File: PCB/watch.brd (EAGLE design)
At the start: 81.1 x 53.1 mm, 58 parts, among them IC1 ISL1209, J2 USB-MICROB, Q1 32.768 KHz, T1 BC850, U2 MKL27Z256VLH4

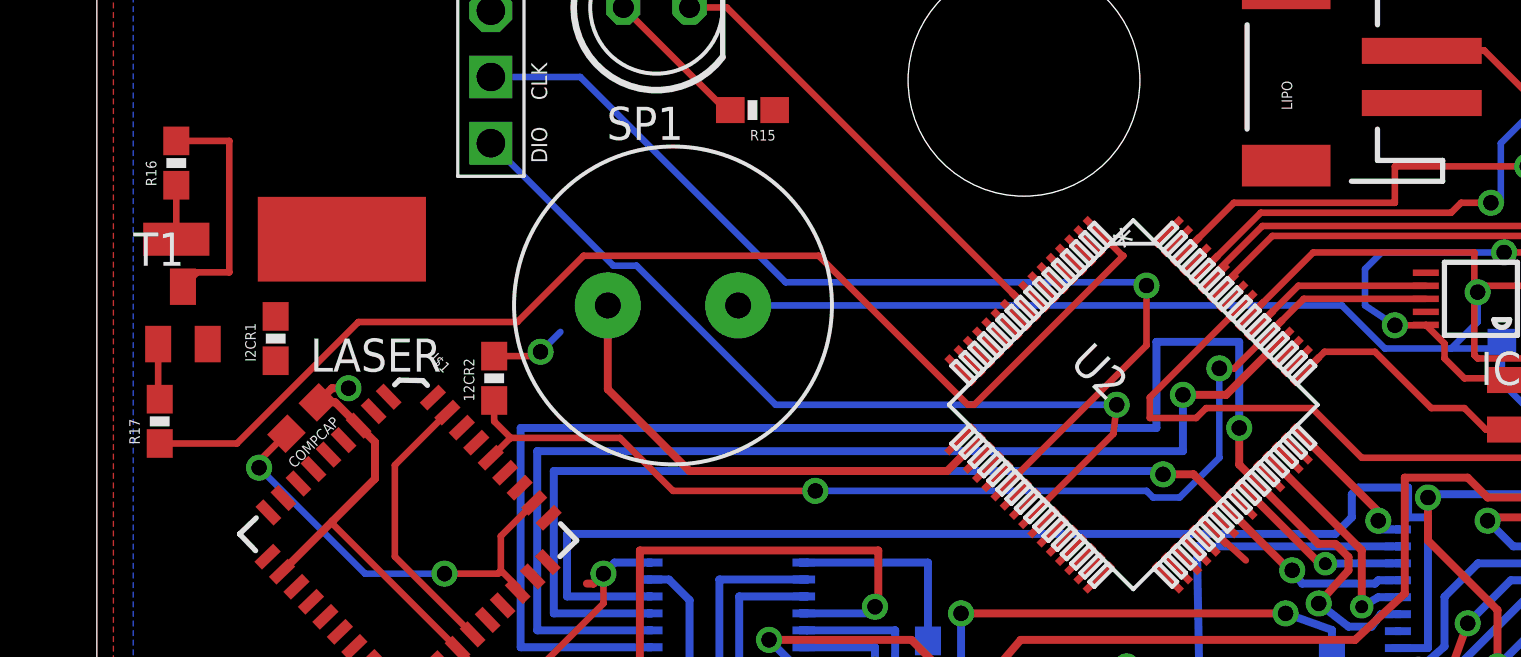
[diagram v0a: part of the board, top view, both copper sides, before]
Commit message: fixed mroe air wires
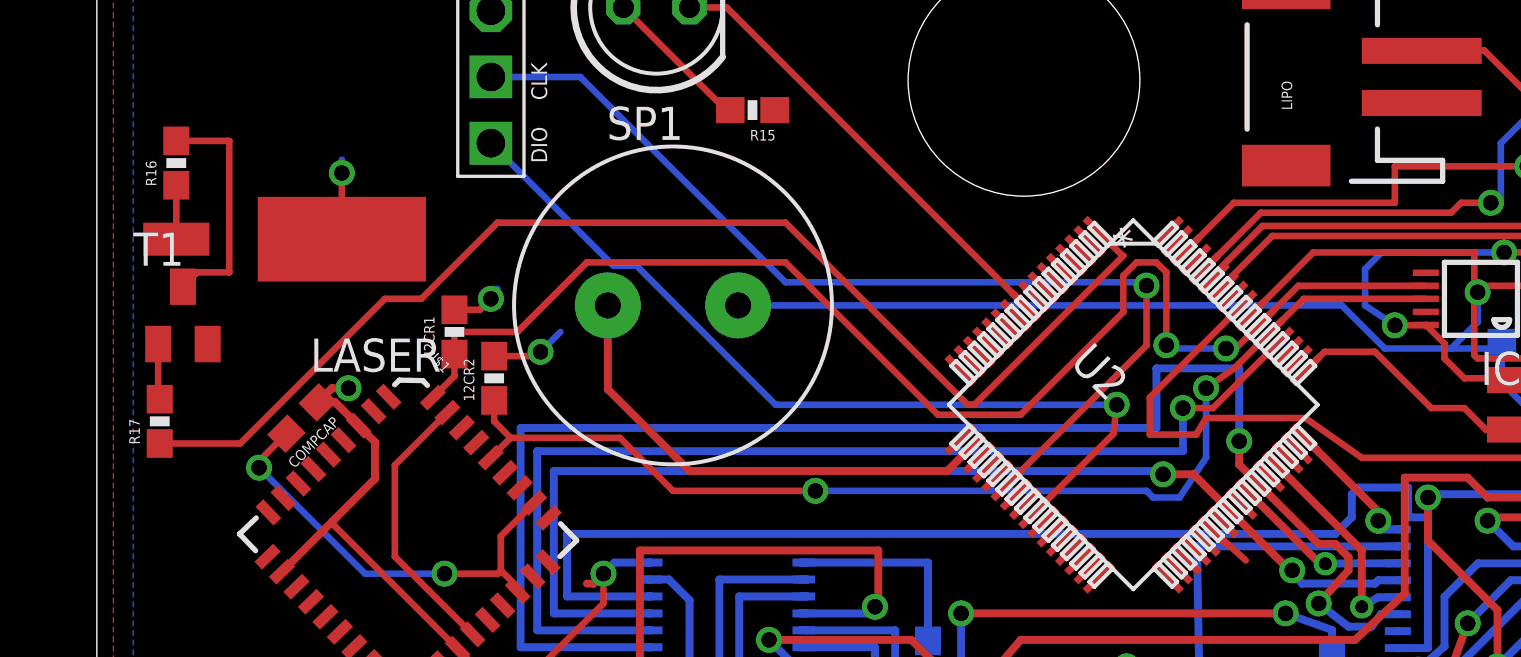
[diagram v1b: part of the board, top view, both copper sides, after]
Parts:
- moved I2CR1 6.86 mm to (24.6, 44.7)
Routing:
- net PTC9: track 6.97 -> 51.0 mm, vias 0 -> 2
- net V+: track 60.1 -> 65.2 mm, vias 7 -> 9
- net PTC0: track 60.0 -> 58.0 mm
- net PTE0: track 46.0 -> 47.0 mm
- net PTC11: track 33.5 -> 34.0 mm

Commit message: wired decoupling caps
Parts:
- moved C6 113.6 mm to (49.8, 48.4), flipped to the bottom, turned to 90 degrees
- moved C5 104.4 mm to (43.6, 46.1), turned to 43.8 degrees
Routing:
- net V+: track 65.2 -> 87.4 mm, vias 9 -> 12
- net GND: track 97.2 -> 113.9 mm, vias 11 -> 13
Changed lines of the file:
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@@
 <attribute name="PROD_ID" value="CAP-00810" x="79.121" y="52.451" size="1.778" layer="27" rot="R90" display="off"/>
 </element>
-<element name="C5" library="SparkFun" package="0603" value=".1uf" x="-57.15" y="73.66"/>
-<element name="C6" library="SparkFun" package="0603" value=".1uf" x="-60.96" y="73.66"/>
+<element name="C5" library="SparkFun" package="0603" value=".1uf" x="43.561" y="46.101" rot="R43.8"/>
+<element name="C6" library="SparkFun" package="0603" value=".1uf" x="49.784" y="48.387" rot="MR90"/>
 <element name="C7" library="SparkFun" package="0603" value=".1uf" x="-64.77" y="73.66"/>
 <element name="C8" library="SparkFun" package="0603" value=".1uf" x="-68.58" y="73.66"/>
@@
 <wire x1="24.257" y1="35.433" x2="26.289" y2="35.433" width="0.254" layer="1"/>
 <wire x1="26.289" y1="35.433" x2="26.416" y2="35.56" width="0.254" layer="1" curve="90"/>
+<wire x1="49.784" y1="47.537" x2="46.189" y2="47.537" width="0.254" layer="16"/>
+<wire x1="46.189" y1="47.537" x2="45.72" y2="48.006" width="0.254" layer="16"/>
+<via x="45.72" y="48.006" extent="1-16" drill="0.6"/>
+<wire x1="45.72" y1="48.006" x2="47.758990625" y2="48.006" width="0.254" layer="1"/>
+<wire x1="47.758990625" y1="48.006" x2="48.286515625" y2="47.478475" width="0.254" layer="1"/>
+<wire x1="42.947503125" y1="45.512678125" x2="42.625321875" y2="45.512678125" width="0.254" layer="1"/>
+<wire x1="42.625321875" y1="45.512678125" x2="40.259" y2="47.879" width="0.254" layer="1"/>
+<via x="40.259" y="47.879" extent="1-16" drill="0.6"/>
+<wire x1="40.259" y1="47.879" x2="41.275" y2="48.768" width="0.254" layer="16"/>
+<wire x1="41.275" y1="48.768" x2="44.196" y2="48.768" width="0.254" layer="16"/>
+<wire x1="44.196" y1="48.768" x2="45.085" y2="48.006" width="0.254" layer="16"/>
+<wire x1="45.085" y1="48.006" x2="45.72" y2="48.006" width="0.254" layer="16"/>
 <wire x1="60.325" y1="44.069" x2="56.94858125" y2="40.23061875" width="0" layer="19" extent="1-16"/>
 <wire x1="48.99361875" y1="35.634415625" x2="56.94858125" y2="40.23061875" width="0" layer="19" extent="1-1"/>
-<wire x1="48.286515625" y1="47.478475" x2="58.674" y2="45.72" width="0" layer="19" extent="1-16"/>
-<wire x1="-58" y1="73.66" x2="15.174" y2="44.239" width="0" layer="19" extent="1-1"/>
-<wire x1="-61.81" y1="73.66" x2="-58" y2="73.66" width="0" layer="19" extent="1-1"/>
-<wire x1="-65.62" y1="73.66" x2="-61.81" y2="73.66" width="0" layer="19" extent="1-1"/>
+<wire x1="-65.62" y1="73.66" x2="15.174" y2="44.239" width="0" layer="19" extent="1-1"/>
 <wire x1="-69.43" y1="73.66" x2="-65.62" y2="73.66" width="0" layer="19" extent="1-1"/>
 </signal>
@@
 <via x="20.32" y="50.8" extent="1-16" drill="0.6"/>
 <wire x1="20.32" y1="50.8" x2="20.32" y2="51.308" width="0.254" layer="16"/>
-<wire x1="45.104521875" y1="44.29648125" x2="48.640065625" y2="47.832028125" width="0" layer="19" extent="1-1"/>
-<wire x1="48.640065625" y1="35.98796875" x2="45.104521875" y2="44.29648125" width="0" layer="19" extent="1-1"/>
-<wire x1="57.302134375" y1="40.584171875" x2="48.640065625" y2="35.98796875" width="0" layer="19" extent="1-1"/>
-<wire x1="60.706" y1="44.958" x2="57.302134375" y2="40.584171875" width="0" layer="19" extent="1-16"/>
+<wire x1="44.17449375" y1="46.68931875" x2="44.17449375" y2="45.226509375" width="0.254" layer="1"/>
+<wire x1="44.17449375" y1="45.226509375" x2="45.104521875" y2="44.29648125" width="0.254" layer="1"/>
+<wire x1="44.17449375" y1="46.68931875" x2="44.11568125" y2="46.68931875" width="0.254" layer="1"/>
+<wire x1="44.11568125" y1="46.68931875" x2="42.799" y2="48.006" width="0.254" layer="1"/>
+<via x="42.799" y="48.006" extent="1-16" drill="0.6"/>
+<wire x1="42.799" y1="48.006" x2="42.545" y2="48.26" width="0.254" layer="16"/>
+<wire x1="49.784" y1="49.237" x2="47.332" y2="49.237" width="0.254" layer="16"/>
+<wire x1="47.332" y1="49.237" x2="47.244" y2="49.149" width="0.254" layer="16"/>
+<via x="47.244" y="49.149" extent="1-16" drill="0.6"/>
+<wire x1="47.244" y1="49.149" x2="47.32309375" y2="49.149" width="0.254" layer="1"/>
+<wire x1="47.32309375" y1="49.149" x2="48.640065625" y2="47.832028125" width="0.254" layer="1"/>
+<wire x1="44.17449375" y1="46.68931875" x2="40.513" y2="50.3508125" width="0.254" layer="1"/>
+<wire x1="40.513" y1="50.3508125" x2="40.513" y2="50.419" width="0.254" layer="1"/>
+<via x="40.513" y="50.419" extent="1-16" drill="0.6"/>
+<wire x1="40.513" y1="50.419" x2="40.64" y2="50.546" width="0.254" layer="16"/>
+<wire x1="40.64" y1="50.546" x2="42.545" y2="50.546" width="0.254" layer="16"/>
+<wire x1="42.545" y1="50.546" x2="43.942" y2="49.149" width="0.254" layer="16"/>
+<wire x1="43.942" y1="49.149" x2="47.244" y2="49.149" width="0.254" layer="16"/>
+<wire x1="45.104521875" y1="44.29648125" x2="48.640065625" y2="35.98796875" width="0" layer="19" extent="1-1"/>
+<wire x1="57.302134375" y1="40.584171875" x2="60.706" y2="44.958" width="0" layer="19" extent="1-16"/>
 <wire x1="41.822" y1="16.002" x2="48.640065625" y2="35.98796875" width="0" layer="19" extent="1-1"/>
 <wire x1="43.649" y1="13.335" x2="41.822" y2="16.002" width="0" layer="19" extent="1-1"/>
@@
 <wire x1="63.666" y1="12.954" x2="43.649" y2="13.335" width="0" layer="19" extent="1-1"/>
 <wire x1="63.666" y1="16.002" x2="63.666" y2="12.954" width="0" layer="19" extent="1-1"/>
-<wire x1="-56.3" y1="73.66" x2="20.32" y2="51.308" width="0" layer="19" extent="1-16"/>
-<wire x1="-60.11" y1="73.66" x2="-56.3" y2="73.66" width="0" layer="19" extent="1-1"/>
-<wire x1="-63.92" y1="73.66" x2="-60.11" y2="73.66" width="0" layer="19" extent="1-1"/>
+<wire x1="-63.92" y1="73.66" x2="20.32" y2="51.308" width="0" layer="19" extent="1-16"/>
 <wire x1="-67.73" y1="73.66" x2="-63.92" y2="73.66" width="0" layer="19" extent="1-1"/>
 </signal>

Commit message: moved IR for smaller form factor
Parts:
- moved LED-IR 4.20 mm to (36.2, 55.4)
- moved R15 3.74 mm to (39.1, 51.1), turned to 270 degrees
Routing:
- net PTE20: track 17.6 -> 13.4 mm
- net N$39: track 5.73 -> 8.71 mm
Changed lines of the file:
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@@
 <element name="LASER" library="Photonics" package="LD-FLUSH-WITH-JUMPER" value="LD" x="20.32" y="48.26" rot="R180"/>
 <element name="LED-E" library="led" package="LED5MM" value="" x="87.884" y="18.034"/>
-<element name="LED-IR" library="led" package="LED5MM" value="" x="32.385" y="57.15"/>
+<element name="LED-IR" library="led" package="LED5MM" value="" x="36.195" y="55.372"/>
 <element name="LED-N" library="led" package="LED5MM" value="" x="82.169" y="26.289"/>
 <element name="LED-S" library="led" package="LED5MM" value="" x="82.169" y="10.922"/>
@@
 <element name="R13" library="SparkFun-Resistors" package="0603-RES" value="220Ohm" x="89.027" y="9.271" rot="R180"/>
 <element name="R14" library="SparkFun-Resistors" package="0603-RES" value="220Ohm" x="72.644" y="12.827" rot="R90"/>
-<element name="R15" library="SparkFun-Resistors" package="0603-RES" value="220Ohm" x="36.068" y="53.213" rot="R180"/>
+<element name="R15" library="SparkFun-Resistors" package="0603-RES" value="220Ohm" x="39.116" y="51.054" rot="R270"/>
 <element name="R16" library="SparkFun-Resistors" package="0603-RES" value="10" x="13.97" y="51.181" rot="R90"/>
 <element name="R17" library="SparkFun-Resistors" package="0603-RES" value="10K" x="13.335" y="41.275" rot="R90"/>
@@
 <contactref element="U2" pad="9"/>
 <contactref element="LED-IR" pad="K"/>
-<wire x1="33.655" y1="57.15" x2="35.079459375" y2="57.15" width="0.254" layer="1"/>
-<wire x1="35.079459375" y1="57.15" x2="46.51875" y2="45.710709375" width="0.254" layer="1"/>
+<wire x1="37.465" y1="55.372" x2="44.831" y2="48.006" width="0.254" layer="1"/>
+<wire x1="44.831" y1="48.006" x2="44.831" y2="47.398459375" width="0.254" layer="1"/>
+<wire x1="44.831" y1="47.398459375" x2="46.51875" y2="45.710709375" width="0.254" layer="1"/>
 </signal>
 <signal name="PTA13">
@@
 <contactref element="R15" pad="2"/>
 <contactref element="LED-IR" pad="A"/>
-<wire x1="31.115" y1="57.15" x2="35.052" y2="53.213" width="0.254" layer="1"/>
-<wire x1="35.052" y1="53.213" x2="35.218" y2="53.213" width="0.254" layer="1"/>
+<wire x1="34.925" y1="55.372" x2="34.925" y2="51.308" width="0.254" layer="1"/>
+<wire x1="34.925" y1="51.308" x2="35.941" y2="50.292" width="0.254" layer="1"/>
+<wire x1="35.941" y1="50.292" x2="39.028" y2="50.292" width="0.254" layer="1"/>
+<wire x1="39.028" y1="50.292" x2="39.116" y2="50.204" width="0.254" layer="1"/>
 </signal>
 <signal name="PTA12">

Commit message: all but one decoup cap done
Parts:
- moved C8 128.9 mm to (56.4, 42.0), flipped to the bottom, turned to 135 degrees
- moved C7 116.5 mm to (45.2, 35.3)
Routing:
- net V+: track 87.4 -> 107.6 mm
- net GND: track 113.9 -> 133.0 mm
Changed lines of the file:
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@@
 <element name="C5" library="SparkFun" package="0603" value=".1uf" x="43.561" y="46.101" rot="R43.8"/>
 <element name="C6" library="SparkFun" package="0603" value=".1uf" x="49.784" y="48.387" rot="MR90"/>
-<element name="C7" library="SparkFun" package="0603" value=".1uf" x="-64.77" y="73.66"/>
-<element name="C8" library="SparkFun" package="0603" value=".1uf" x="-68.58" y="73.66"/>
+<element name="C7" library="SparkFun" package="0603" value=".1uf" x="45.212" y="35.306"/>
+<element name="C8" library="SparkFun" package="0603" value=".1uf" x="56.388" y="42.037" rot="MR135"/>
 <element name="COMPCAP" library="SparkFun" package="0603" value=".1uf" x="18.796" y="41.402" rot="R225"/>
 <element name="DISP1" library="SparkFun-Displays" package="DIL12" value="7-SEGMENT-4DIGIT-COUNTER-HP-BUBBLE" x="44.069" y="25.273">
@@
 <wire x1="44.196" y1="48.768" x2="45.085" y2="48.006" width="0.254" layer="16"/>
 <wire x1="45.085" y1="48.006" x2="45.72" y2="48.006" width="0.254" layer="16"/>
+<wire x1="44.958" y1="34.417" x2="47.776203125" y2="34.417" width="0.254" layer="1"/>
+<wire x1="47.776203125" y1="34.417" x2="48.99361875" y2="35.634415625" width="0.254" layer="1"/>
+<wire x1="44.362" y1="35.306" x2="44.362" y2="35.013" width="0.254" layer="1"/>
+<wire x1="44.362" y1="35.013" x2="44.958" y2="34.417" width="0.254" layer="1"/>
+<wire x1="44.362" y1="35.013" x2="43.18" y2="35.013" width="0.254" layer="1"/>
+<wire x1="43.18" y1="35.013" x2="43.18" y2="33.401" width="0.254" layer="1"/>
+<wire x1="43.18" y1="33.401" x2="37.465" y2="33.401" width="0.254" layer="1"/>
+<wire x1="37.465" y1="33.401" x2="36.957" y2="33.909" width="0.254" layer="1"/>
+<wire x1="36.957" y1="33.909" x2="35.941" y2="33.909" width="0.254" layer="1"/>
+<wire x1="35.941" y1="33.909" x2="35.56" y2="33.528" width="0.254" layer="1"/>
+<wire x1="35.56" y1="33.528" x2="35.56" y2="31.877" width="0.254" layer="1"/>
+<wire x1="35.56" y1="31.877" x2="35.814" y2="31.623" width="0.254" layer="1"/>
+<wire x1="35.814" y1="31.623" x2="36.449" y2="31.623" width="0.254" layer="1"/>
 <wire x1="60.325" y1="44.069" x2="56.94858125" y2="40.23061875" width="0" layer="19" extent="1-16"/>
-<wire x1="48.99361875" y1="35.634415625" x2="56.94858125" y2="40.23061875" width="0" layer="19" extent="1-1"/>
-<wire x1="-65.62" y1="73.66" x2="15.174" y2="44.239" width="0" layer="19" extent="1-1"/>
-<wire x1="-69.43" y1="73.66" x2="-65.62" y2="73.66" width="0" layer="19" extent="1-1"/>
+<wire x1="55.786959375" y1="41.43595625" x2="15.174" y2="44.239" width="0" layer="19" extent="1-1"/>
 </signal>
 <signal name="V+">
@@
 <wire x1="42.545" y1="50.546" x2="43.942" y2="49.149" width="0.254" layer="16"/>
 <wire x1="43.942" y1="49.149" x2="47.244" y2="49.149" width="0.254" layer="16"/>
-<wire x1="45.104521875" y1="44.29648125" x2="48.640065625" y2="35.98796875" width="0" layer="19" extent="1-1"/>
+<wire x1="47.958096875" y1="35.306" x2="48.640065625" y2="35.98796875" width="0.254" layer="1"/>
+<wire x1="46.062" y1="35.306" x2="47.958096875" y2="35.306" width="0.254" layer="1"/>
+<wire x1="46.062" y1="35.306" x2="44.538" y2="36.83" width="0.254" layer="1"/>
+<wire x1="44.538" y1="36.83" x2="31.115" y2="36.83" width="0.254" layer="1"/>
+<wire x1="31.115" y1="36.83" x2="30.353" y2="36.068" width="0.254" layer="1"/>
+<wire x1="30.353" y1="36.068" x2="30.353" y2="35.433" width="0.254" layer="1"/>
+<wire x1="63.666" y1="12.954" x2="63.666" y2="16.002" width="0" layer="19" extent="1-1"/>
+<wire x1="43.649" y1="13.335" x2="63.666" y2="12.954" width="0" layer="19" extent="1-1"/>
+<wire x1="43.649" y1="10.414" x2="43.649" y2="13.335" width="0" layer="19" extent="1-1"/>
+<wire x1="41.822" y1="16.002" x2="43.649" y2="13.335" width="0" layer="19" extent="1-1"/>
+<wire x1="46.062" y1="35.306" x2="41.822" y2="16.002" width="0" layer="19" extent="1-1"/>
 <wire x1="57.302134375" y1="40.584171875" x2="60.706" y2="44.958" width="0" layer="19" extent="1-16"/>
-<wire x1="41.822" y1="16.002" x2="48.640065625" y2="35.98796875" width="0" layer="19" extent="1-1"/>
-<wire x1="43.649" y1="13.335" x2="41.822" y2="16.002" width="0" layer="19" extent="1-1"/>
-<wire x1="43.649" y1="10.414" x2="43.649" y2="13.335" width="0" layer="19" extent="1-1"/>
-<wire x1="63.666" y1="12.954" x2="43.649" y2="13.335" width="0" layer="19" extent="1-1"/>
-<wire x1="63.666" y1="16.002" x2="63.666" y2="12.954" width="0" layer="19" extent="1-1"/>
-<wire x1="-63.92" y1="73.66" x2="20.32" y2="51.308" width="0" layer="19" extent="1-16"/>
-<wire x1="-67.73" y1="73.66" x2="-63.92" y2="73.66" width="0" layer="19" extent="1-1"/>
+<wire x1="56.98904375" y1="42.638040625" x2="20.32" y2="51.308" width="0" layer="19" extent="1-16"/>
 </signal>
 <signal name="PTA19">
@@
 <wire x1="66.675" y1="39.878" x2="59.436" y2="39.878" width="0.254" layer="1"/>
 <wire x1="59.436" y1="39.878" x2="57.277" y2="41.402" width="0.254" layer="1"/>
-<wire x1="57.277" y1="41.402" x2="53.467" y2="41.402" width="0.254" layer="1"/>
 <wire x1="53.467" y1="41.402" x2="53.086" y2="40.767" width="0.254" layer="1"/>
 <wire x1="53.086" y1="40.767" x2="51.308" y2="40.767" width="0.254" layer="1"/>
@@
 <wire x1="69.215" y1="37.338" x2="69.215" y2="32.85" width="0.254" layer="1"/>
 <wire x1="69.215" y1="32.85" x2="72.51" y2="32.85" width="0.254" layer="1"/>
+<wire x1="57.277" y1="41.402" x2="53.467" y2="41.402" width="0.254" layer="1"/>
 </signal>
 <signal name="PTC4">
@@
 <contactref element="T2" pad="B"/>
 <wire x1="64.94" y1="40.96" x2="64.196" y2="40.96" width="0.254" layer="1"/>
-<wire x1="64.196" y1="40.96" x2="63.373" y2="41.783" width="0.254" layer="1"/>
-<wire x1="63.373" y1="41.783" x2="62.103" y2="41.783" width="0.254" layer="1"/>
 <wire x1="57.302134375" y1="43.235825" x2="58.008309375" y2="43.942" width="0.254" layer="1"/>
-<wire x1="58.008309375" y1="43.942" x2="59.944" y2="43.942" width="0.254" layer="1"/>
-<wire x1="59.944" y1="43.942" x2="62.103" y2="41.783" width="0.254" layer="1"/>
+<wire x1="58.008309375" y1="43.942" x2="61.214" y2="43.942" width="0.254" layer="1"/>
+<wire x1="61.214" y1="43.942" x2="64.196" y2="40.96" width="0.254" layer="1"/>
 </signal>
 </signals>
